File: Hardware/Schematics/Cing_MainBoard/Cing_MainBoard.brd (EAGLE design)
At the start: 100 x 100 mm, 116 parts, among them IC1 L293D, IC3 FT232RL, Q1 16mhz, Q2 BSS138, Q3 BSS138, Q4 BSS138, Q5 BSS138, U2 BMP180, U3 MPU-6050MPU6050

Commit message: commit
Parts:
- removed R8, R9: 1k, rcl:R1206
- removed U$8: BATTERY_18650-HOLDER, Cing Library:BATTERY_18650-HOLDER
- added BT1: (no value), Cing Library:BATTERY-AA-KIT
- added IC2, IC4: Attiny85, Cing Library:8S2
- added LED2: Empty, led:1206
- added M1: ELECTRET_MICROPHON-F6035AP, microphon:F6035AP
- added Q6: BSS138, Cing Library:SOT23
- added R42, R44, R45: 10k, rcl:R1206
- added R43: 100, rcl:R1206
- added SP1: AL11P, buzzer:AL11P
- added YELLOW1: Full, led:1206
- moved R41 6.58 mm to (-29.1, -38.1), turned to 90 degrees
- moved C12 5.37 mm to (-20.9, -37.7), turned to 0 degrees
- moved C10 2.82 mm to (-21.4, -47.3), flipped to the bottom, turned to 0 degrees
- moved C9 0.92 mm to (-1.20, 44.2)
- moved C11 0.60 mm to (18.4, -46.9)
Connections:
- removed net N$3: R8.1, U$1.D1
- removed net N$6: R9.1, U$1.D0
- new net N$21: IC2.6, LED2.A
- new net N$28: Q6.3, SP1.-
- new net N$30: LED2.C, R43.1, YELLOW1.C
- new net N$37: IC2.3, YELLOW1.A
- new net N$38: IC4.6, Q6.1, R45.1
- new net VOLTAGE_SENSE: IC2.2, R42.2, R44.1
- net +3V3: now also IC2.8, IC4.8, SP1.+
- net GND: now also BT1.GND@1, IC2.4, IC4.4, Q6.2, R43.2, R44.2, R45.2; no longer U$8.GND@1, U$8.GND@2, U$8.GND@3
- net IRFU: now also BT1.PWR@1, R42.1; no longer U$8.PWR@1, U$8.PWR@2, U$8.PWR@3
- net RXD: now also U$1.D0; no longer R9.2
- net SCL: now also IC2.7, IC4.7
- net SDA: now also IC2.5, IC4.5
- net TXD: now also U$1.D1; no longer R8.2
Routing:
- net SCL: track 42.5 -> 165.5 mm, vias 0 -> 3
- net SDA: track 49.4 -> 167.4 mm, vias 2 -> 7
- net GND: track 598.0 -> 652.8 mm, vias 28 -> 29
- net +3V3: track 665.3 -> 704.4 mm, vias 36 -> 40
- net N$38: track 0.00 -> 19.8 mm, vias 0 -> 2
- net N$30: track 0.00 -> 10.3 mm
- net VOLTAGE_SENSE: track 0.00 -> 8.09 mm, vias 0 -> 1
- net TXD: track 114.8 -> 121.9 mm
- net IN_A2: track 115.0 -> 108.2 mm
- net N$21: track 0.00 -> 5.48 mm
- net MOSI: track 95.5 -> 90.3 mm
- net N$37: track 0.00 -> 5.12 mm
- net N$40: track 73.9 -> 69.3 mm
- net IN_B2: track 44.6 -> 40.1 mm
- net IN_A1: track 123.6 -> 119.1 mm
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
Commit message: commit
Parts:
- added JP1: (no value), pinhead:1X03
- added LED10, LED11, LED4, LED9: WS2812B3535, adafruit:LED3535
- moved LED7 1.80 mm to (34.3, 34.3)
- moved LED6 1.27 mm to (-34.3, 34.3)
- moved C13 1.12 mm to (39.8, 30.4)
- moved U$21 0.71 mm to (-25.5, 25.5)
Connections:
- new net N$41: JP1.2, LED11.3, LED8.2
- net +3V3: now also JP1.1, LED10.2, LED11.2, LED4.2, LED9.2
- net GND: now also JP1.3, LED10.4, LED11.4, LED4.4, LED9.4
- net N$1: now also LED10.3, LED9.1
- net N$11: now also LED11.1, LED4.3
- net N$12: now also LED10.1
- net N$2: now also LED4.1, LED9.3
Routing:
- net +3V3: track 704.4 -> 730.0 mm
- net GND: track 652.8 -> 671.5 mm
- net N$41: track 0.00 -> 8.19 mm
- net N$2: track 80.0 -> 85.5 mm
- net N$11: track 100.2 -> 103.4 mm
- net N$12: track 7.38 -> 8.96 mm
- net VCC_MOT: track 123.0 -> 124.0 mm
- net BAT+: track 216.5 -> 215.8 mm

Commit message: commit
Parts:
- removed D2: CGRM4007-G, diode:SOD-123_MINI-SMA
- removed LED2: Empty, led:1206
- removed R42, R44: 10k, rcl:R1206
- removed R43: 100, rcl:R1206
- removed U$21: DC-DC-STEP-UP-MT3608, Cing Library:DC-DC-STEP-UP-MT3608
- removed U2: BMP180, Cing Library:BMP180
- removed YELLOW1: Full, led:1206
- added 1, 8205: 8205, FS8205A:TSSOP-8
- added C14, C15: 22uf, rcl:C1206
- added C16: 100n, rcl:C1206
- added C17: (no value), rcl:E3,5-8
- added D3: (no value), adafruit:SMADIODE
- added IC5: BME280, bosch-bme280:BME280
- added L1: DR125, inductors:DR125
- added L2: DR127, inductors:DR127
- added R46, R47, R8: 1k, rcl:R1206
- added R48: 100, rcl:R1206
- added R49: 7k5, rcl:R1206
- added R9: 12k, rcl:R1206
- added SJ1: (no value), jumper:SJW
- added SJ2: (no value), jumper:SJ
- added U$13: ADS1015IDGT, bt_adc:MSOP10_0.5
- added U$5: MT3608SOT23-6, MT3608:SOT23-6
- added U$8: DW01, DW01:SOT23-6
- added U$9: LM1117, Cing Library:LM1117
- D1: value CGRM4007-G -> (none); device diode:SOD-123_MINI-SMA -> adafruit:SMADIODE
- IC2: value Attiny85 -> LM2576S; device Cing Library:8S2 -> lm2576:TO263-5
- R4: value 1k2 -> 1k
- R41: value 10k -> 2; device rcl:R1206 -> rcl:R2512
- moved IC2 76.3 mm to (-33.4, 31.9), flipped to the bottom
- moved IC4 59.8 mm to (-75.5, 27.1)
- moved D1 57.8 mm to (-27.4, 25.1), turned to 90 degrees
- moved Q6 52.0 mm to (-76.2, 36.4)
- moved R45 44.6 mm to (-66.6, 33.2)
- moved SP1 44.4 mm to (-70.4, 45.2)
- moved U3 21.5 mm to (0.00, 5.66)
- moved R41 14.9 mm to (-15.3, -32.5), turned to 180 degrees
- moved C11 9.67 mm to (8.78, -46.0), turned to 270 degrees
- moved R30 7.10 mm to (13.5, 19.4)
- moved JP2 6.00 mm to (-28.5, 47.3)
- moved JP3 5.70 mm to (-20.7, 47.3)
- moved U$6 5.69 mm to (-34.7, 15.4), turned to 90 degrees
- moved C12 2.28 mm to (-22.0, -35.7)
- moved C10 0.71 mm to (-21.3, -48.0)
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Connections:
- removed net N$23: D1.A, D2.C, R41.1, TP4056.5
- removed net N$30: LED2.C, R43.1, YELLOW1.C
- removed net N$37: IC2.3, YELLOW1.A
- removed net VOLTAGE_SENSE: IC2.2, R42.2, R44.1
- new net BAT-: 1.2, 1.3, 8205.2, 8205.3, BT1.GND@1, C16.2, U$7.-, U$8.6
- new net CUR-SENSE: R22.1, R41.2, SW5.CH1B, SW5.CH2B, U$13.6
- new net N$3: 1.1, 1.8
- new net N$35: R46.1, R49.2, R9.2, U$5.P$3
- new net N$44: D3.A, L1.2, U$5.P$1
- new net N$46: C14.1, D3.C, R49.1, R9.1, SJ1.1
- new net N$47: 8205.1, 8205.8
- new net N$48: 1.4, 8205.4, U$8.1
- new net N$49: 1.5, 8205.5, U$8.3
- new net N$50: C16.1, R48.1, U$8.5
- new net N$54: R47.1, U$8.2
- new net N$6: R4.2, R8.1
- new net VCC_SERVO: C17.+, IC2.4, JP2.2, JP3.2, JP4.2, L2.2
- new net VDD: U$13.8, U$9.2, U$9.TAB
- net +3V3: now also IC5.2, IC5.6, IC5.8; no longer IC2.8, U2.2, U2.3
- net BAT+: now also C15.1, L1.1, R41.1, R48.2, U$13.4, U$13.7, U$5.P$4, U$5.P$5, U$9.3; no longer R22.1, SW5.CH1B, SW5.CH2B, U$21.IN+
- net GND: now also 1.6, 1.7, 8205.6, 8205.7, C14.2, C15.2, C17.-, D1.A, IC2.3, IC5.1, IC5.5, IC5.7, R46.2, R47.2, R8.2, U$13.1, U$13.3, U$13.5, U$5.P$2, U$9.1; no longer BT1.GND@1, D2.A, IC2.4, R4.2, R43.2, R44.2, U$21.IN-, U$21.OUT-, U$7.-, U2.7
- net IRFU: now also SJ2.1; no longer D1.C, R41.2, R42.1
- net N$21: now also D1.C, IC2.2, L2.1; no longer IC2.6, LED2.A
- net N$26: now also SJ2.2, TP4056.5
- net SCL: now also IC5.4, U$13.10; no longer IC2.7, U2.5
- net SDA: now also IC5.3, U$13.9; no longer IC2.5, U2.6
- net VCC_MOT: now also IC2.1, SJ1.2; no longer JP2.2, JP3.2, JP4.2, U$21.OUT+
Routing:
- net GND: track 671.5 -> 849.3 mm, vias 29 -> 33
- net VCC_SERVO: track 0.00 -> 117.3 mm, vias 0 -> 3
- net BAT-: track 0.00 -> 93.6 mm, vias 0 -> 1
- net VCC_MOT: track 124.0 -> 34.2 mm, vias 4 -> 2
- net BAT+: track 215.8 -> 259.4 mm, vias 9 -> 10
- net N$50: track 0.00 -> 42.8 mm
- net +3V3: track 730.0 -> 693.9 mm, vias 40 -> 35
- net CUR-SENSE: track 0.00 -> 27.5 mm, vias 0 -> 3
- net N$23: track 27.0 -> 0.00 mm, vias 1 -> 0
- net N$46: track 0.00 -> 25.6 mm, vias 0 -> 2
- net N$54: track 0.00 -> 20.1 mm, vias 0 -> 2
- net SDA: track 167.4 -> 147.4 mm
- net N$38: track 19.8 -> 0.15 mm, vias 2 -> 0
- net VDD: track 0.00 -> 19.5 mm, vias 0 -> 3
- net N$49: track 0.00 -> 17.6 mm, vias 0 -> 1
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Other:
- board text removed: "Button"
- board text removed: "Header1"
- board text removed: "Header2"
- board text removed: "Light Sensor"

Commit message: commit
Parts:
- removed IC4: Attiny85, Cing Library:8S2
- removed M1: ELECTRET_MICROPHON-F6035AP, microphon:F6035AP
- removed Q6: BSS138, Cing Library:SOT23
- removed R45: 10k, rcl:R1206
- removed SP1: AL11P, buzzer:AL11P
- added U$14: RANGING-SENSOR-VL53L0X, diy-modules:RANGING-SENSOR-VL53L0X
- U$16: value 3.3V -> BAT+
- U$9: value LM1117 -> LM1117-5V
- moved C15 22.1 mm to (-12.6, 27.2), flipped to the top, turned to 225 degrees
- moved C9 14.2 mm to (-5.62, 30.7)
- moved C4 14.1 mm to (-8.82, 22.7), turned to 225 degrees
- moved U$22 12.3 mm to (17.3, 44.1)
- moved VERSION 2.00 mm to (49.5, 0.00)
- moved IC2 0.76 mm to (-34.2, 31.9)
- moved U$9 0.20 mm to (-31.2, -44.4)
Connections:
- removed net N$28: Q6.3, SP1.-
- removed net N$38: IC4.6, Q6.1, R45.1
- net +3V3: no longer IC4.8, SP1.+, U$16.LEGO
- net BAT+: now also U$16.LEGO
- net GND: now also U$14.2; no longer IC4.4, Q6.2, R45.2
- net SCL: now also U$14.3; no longer IC4.7
- net SDA: now also U$14.4; no longer IC4.5
- net VDD: now also U$14.1
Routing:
- net VDD: track 19.5 -> 163.1 mm, vias 3 -> 6
- net BAT+: track 259.4 -> 299.4 mm, vias 10 -> 12
- net SDA: track 147.4 -> 180.8 mm
- net SCL: track 149.5 -> 181.9 mm, vias 3 -> 5
- net CUR-SENSE: track 27.5 -> 53.8 mm, vias 3 -> 4
- net +3V3: track 693.9 -> 675.5 mm
- net GND: track 849.3 -> 841.5 mm, vias 33 -> 35
- net RXD: track 103.2 -> 106.6 mm
- net TXD: track 117.5 -> 120.7 mm
- net D2: track 41.3 -> 44.4 mm
- net D3: track 51.7 -> 54.7 mm
- net N$2: track 91.7 -> 88.7 mm
- net D4: track 106.4 -> 109.3 mm
- net D5: track 86.0 -> 88.8 mm
- net D6: track 100.9 -> 103.6 mm
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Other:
- board text added: "1"
- board text added: "2"
- board text added: "ICSP"

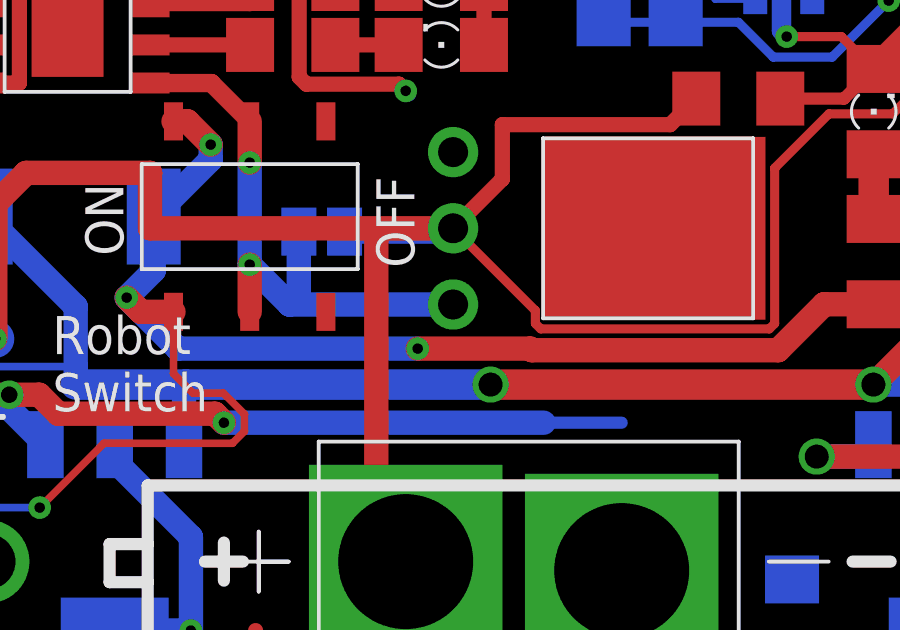
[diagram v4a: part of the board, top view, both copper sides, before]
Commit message: Adding better P-fet
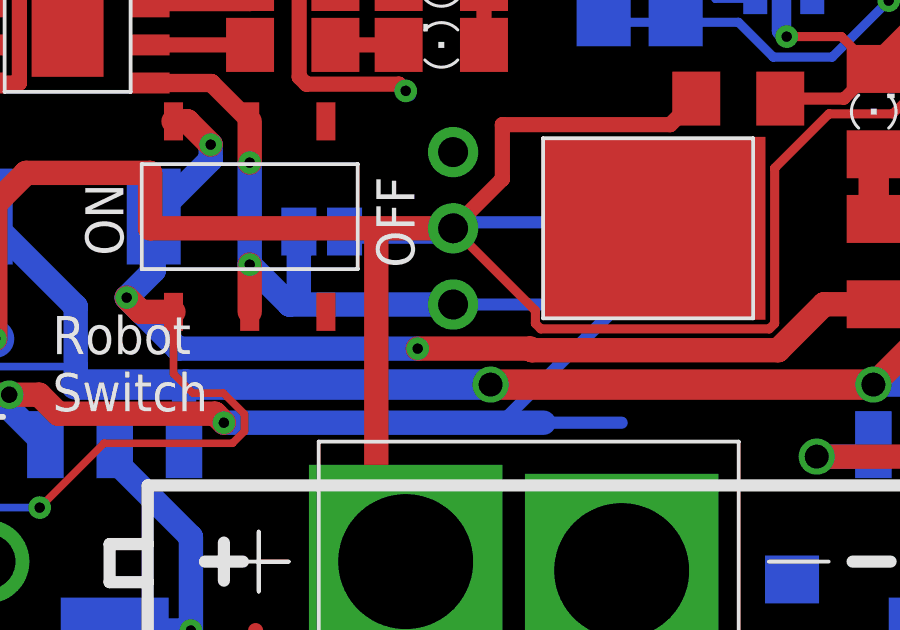
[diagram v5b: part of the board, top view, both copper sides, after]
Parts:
- added Q7: NP2301AMR-G, transistor-fet:SC75_INFINEON
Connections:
- net GND: now also Q7.1
- net IRFU: now also Q7.2
- net N$26: now also Q7.3
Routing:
- net GND: track 841.5 -> 860.7 mm
- net N$26: track 20.1 -> 27.8 mm
- net IRFU: track 91.6 -> 97.5 mm
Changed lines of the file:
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@@
 <attribute name="VALUE" x="23.15" y="-4.445" size="1.27" layer="27" rot="R180"/>
+</element>
+<element name="Q7" library="transistor-fet" library_urn="urn:adsk.eagle:library:396" package="SC75_INFINEON" package3d_urn="urn:adsk.eagle:package:28542/1" value="NP2301AMR-G" x="3.6576" y="-32.6898" smashed="yes" rot="MR270">
+<attribute name="NAME" x="2.6576" y="-31.8898" size="1.27" layer="26" rot="MR270"/>
+<attribute name="VALUE" x="5.9576" y="-31.8898" size="1.27" layer="28" rot="MR270"/>
 </element>
 </elements>
@@
 <wire x1="-20.2348" y1="20.8176875" x2="-20.2348" y2="19.2278" width="0.508" layer="1"/>
 <wire x1="-16.510409375" y1="20.505503125" x2="-18.608940625" y2="22.604034375" width="0.508" layer="1"/>
+<contactref element="Q7" pad="1"/>
+<wire x1="4.9132" y1="-32.84250625" x2="4.9132" y2="-33.53709375" width="0.4064" layer="16"/>
+<wire x1="4.70169375" y1="-32.631" x2="4.9132" y2="-32.84250625" width="0.4064" layer="16"/>
+<wire x1="4.2326" y1="-32.1898" x2="4.6738" y2="-32.631" width="0.4064" layer="16"/>
+<wire x1="4.6738" y1="-32.631" x2="4.70169375" y2="-32.631" width="0.4064" layer="16"/>
+<wire x1="4.9132" y1="-33.53709375" x2="-0.91970625" y2="-39.37" width="0.4064" layer="16"/>
+<wire x1="-0.91970625" y1="-39.37" x2="-10.16" y2="-39.37" width="0.4064" layer="16"/>
 </signal>
 <signal name="N$7">
@@
 <wire x1="-6.138" y1="-33" x2="-2.63" y2="-33" width="0.8128" layer="16"/>
 <wire x1="-2.63" y1="-33" x2="-2.52" y2="-32.89" width="0.8128" layer="16"/>
+<contactref element="Q7" pad="2"/>
+<wire x1="3.0826" y1="-32.6898" x2="-2.3198" y2="-32.6898" width="0.4064" layer="16"/>
+<wire x1="-2.3198" y1="-32.6898" x2="-2.63" y2="-33" width="0.4064" layer="16"/>
 </signal>
 <signal name="N$9">
@@
 <wire x1="-9.3" y1="-29.325" x2="-10.578" y2="-28.047" width="0.6096" layer="1"/>
 <wire x1="-10.578" y1="-28.047" x2="-12.62" y2="-28.047" width="0.6096" layer="1"/>
+<contactref element="Q7" pad="3"/>
+<wire x1="4.2326" y1="-33.1898" x2="1.9924" y2="-35.43" width="0.4064" layer="16"/>
+<wire x1="1.9924" y1="-35.43" x2="-2.52" y2="-35.43" width="0.4064" layer="16"/>
 </signal>
 <signal name="N$41">

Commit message: commit
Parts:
- added Q6: NP2301AMR-G, transistor-fet:SC75_INFINEON
- added U$15: (no value), diy-modules:COMPASS-HMC5883L
- moved Q7 0.09 mm to (3.66, -32.6)
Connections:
- net +3V3: now also U$15.1
- net GND: now also Q6.1, U$15.2
- net IRFU: now also Q6.2
- net N$26: now also Q6.3
- net SCL: now also U$15.3
- net SDA: now also U$15.4
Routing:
- net SDA: track 180.8 -> 205.1 mm, vias 7 -> 8
- net SCL: track 181.9 -> 199.7 mm, vias 5 -> 7
- net IRFU: track 97.5 -> 100.4 mm, vias 1 -> 2
- net N$26: track 27.8 -> 29.3 mm
- net GND: track 860.7 -> 859.3 mm, vias 35 -> 36

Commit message: commit
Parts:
- moved C9 40.3 mm to (-45.6, 35.0), turned to 315 degrees
- moved C4 25.0 mm to (-27.1, 39.7), turned to 315 degrees
- moved C6 24.5 mm to (36.1, 39.3), turned to 0 degrees
- moved JP4 14.8 mm to (27.3, 45.3)
- moved R26 13.6 mm to (38.4, 34.7), turned to 90 degrees
- moved R29 10.6 mm to (33.1, 42.9), turned to 270 degrees
- moved C5 8.61 mm to (34.3, 34.3)
- moved SW6 7.90 mm to (-45.4, 18.4)
- moved C17 7.58 mm to (-41.1, 27.9), turned to 135 degrees
- renumbered JP1 to WS2812
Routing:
- net GND: track 859.3 -> 794.4 mm, vias 36 -> 35
- net +3V3: track 675.5 -> 646.6 mm, vias 35 -> 36
- net SCK: track 155.4 -> 139.5 mm
- net D6: track 103.6 -> 117.9 mm, vias 2 -> 3
- net N$42: track 20.3 -> 9.25 mm
- net N$4: track 36.7 -> 27.0 mm
- net A6: track 150.7 -> 141.5 mm, vias 7 -> 4
- net N$1: track 101.5 -> 94.6 mm, vias 4 -> 2
- net VCC_MOT: track 34.5 -> 28.3 mm, vias 2 -> 1
- net IN_A1: track 122.3 -> 116.9 mm
- net N$2: track 88.7 -> 92.0 mm
- net SCL: track 199.7 -> 197.7 mm, vias 7 -> 6
- net VCC_SERVO: track 116.3 -> 114.7 mm, vias 3 -> 2
- net N$11: track 103.4 -> 102.0 mm
- net SDA: track 205.1 -> 203.9 mm, vias 8 -> 7
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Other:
- board text added: "Created by RobotCing Team: Veronika Nemjová Stanley Jochman Designed in Slovakia Sponsored by PCBWay"
- board text removed: "Created by RobotCing Team: Veronika Nemjová Stanislav Jochman Designed in Slovakia"

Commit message: commit
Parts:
- added C18, C19, C20: 100n, rcl:C1206
- added JP1, JP10, JP11, JP12, JP13, JP14, JP15, JP16, JP17, JP18, JP19, JP20, JP21, JP22, JP6, JP7, JP8, JP9: (no value), pinhead:1X01
- added R42, R43: 10k, rcl:R1206
- added SW7: (no value), Cing Library:USB_SWITCH
- added U$21: SX1509, Cing Library:QFN28
- added U$23: WIRELESS-BLUETOOTH-HC-05, Cing Library:WIRELESS-BLUETOOTH-HC-05
- moved U$15 20.2 mm to (24.2, 40.3)
- moved C15 6.59 mm to (-10.2, 21.0)
- moved JP4 3.36 mm to (30.0, 47.3)
- moved R32 2.22 mm to (31.8, -47.5)
- moved R34 1.12 mm to (-19.1, -16.9)
- turned R21 to 270 degrees
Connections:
- new net A0H: SW7.COM1, U$2.A0
- new net N$23: R42.2, U$21.9
- new net N$28: R43.1, U$21.23
- new net N$30: JP1.1, U$21.7
- new net N$37: JP6.1, U$21.6
- new net N$38: JP7.1, U$21.5
- new net N$51: JP8.1, U$21.1
- new net N$52: JP9.1, U$21.2
- new net N$53: JP10.1, U$21.28
- new net N$55: JP11.1, U$21.27
- new net N$56: JP12.1, U$21.21
- new net N$57: JP13.1, U$21.20
- new net N$58: JP14.1, U$21.19
- new net N$59: JP15.1, U$21.15
- new net N$60: JP16.1, U$21.14
- new net N$61: JP17.1, U$21.13
- new net N$62: JP18.1, U$21.8
- new net N$63: JP19.1, U$21.16
- new net N$64: JP20.1, U$21.22
- new net N$65: C18.2, IC3.3
- new net N$66: R23.2, R29.1, SW7.CH1A
- net +3V3: now also C19.1, C20.1, JP21.1, JP22.1, R42.1, R43.2, U$21.12, U$21.18, U$21.4
- net A0: now also SW7.CH1B; no longer U$2.A0
- net A6: no longer R23.2, R29.1
- net BAT+: now also U$23.5
- net D2: now also U$23.3
- net D5: now also U$23.2
- net GND: now also C19.2, C20.2, U$21.10, U$21.17, U$21.26, U$21.3, U$23.4
- net RESET: now also C18.1
- net SCL: now also U$21.25
- net SDA: now also U$21.24
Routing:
- net A6: track 141.5 -> 32.9 mm, vias 4 -> 1
- net GND: track 794.4 -> 896.0 mm, vias 35 -> 36
- net A0H: track 0.00 -> 57.6 mm, vias 0 -> 5
- net A0: track 20.6 -> 78.1 mm, vias 0 -> 9
- net N$57: track 0.00 -> 30.5 mm
- net N$56: track 0.00 -> 29.2 mm
- net +3V3: track 646.6 -> 674.2 mm, vias 36 -> 39
- net N$58: track 0.00 -> 25.5 mm
- net SCL: track 197.7 -> 223.0 mm, vias 6 -> 7
- net SDA: track 203.9 -> 225.4 mm
- net N$63: track 0.00 -> 17.8 mm
- net N$59: track 0.00 -> 16.2 mm
- net N$61: track 0.00 -> 12.8 mm
- net N$60: track 0.00 -> 12.2 mm
- net N$65: track 0.00 -> 10.6 mm, vias 0 -> 2
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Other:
- board text added: "BT"
- board text added: "Header 3"
